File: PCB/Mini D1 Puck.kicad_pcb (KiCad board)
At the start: 2 copper layers, 32 x 36 mm, 14 parts, among them J1 PinHeader_1x03_P2.54mm_Vertic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, Q1 2N2222, Q2 2n2222, SW1 SW_Slide_SPDT_Angled_CK_OS102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, U1 D1_mini_board

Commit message: PCB fixes/reset button
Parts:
- added R6: 10K, Resistor_THT:R_Axial_DIN0204_L3.6mm_D1.6mm_P5.08mm_Horizontal, F.Cu at (171.5, 83.0)
- added SW2: SW_PUSH_1P1T_6x3.5mm_H4.3_APEM_MJTP1243, Button_Switch_THT:SW_PUSH_1P1T_6x3.5mm_H4.3_APEM_MJTP1243, F.Cu at (192.8, 83.0)
- moved C1 0.50 mm to (192.8, 76.0)
- moved R1 0.50 mm to (197.0, 70.5)
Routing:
- net (no net): track 277.9 -> 342.8 mm

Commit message: PCB Update. These gerber files were ordered May 1 2025
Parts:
- removed the B at (181.8, 59.5)
- added B: , Connector_JST:JST_EH_S3B-EH_1x03_P2.50mm_Horizontal, F.Cu at (182.0, 59.5)
- moved M 2.50 mm to (193.2, 59.5)
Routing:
- net (no net): track 342.8 -> 363.3 mm

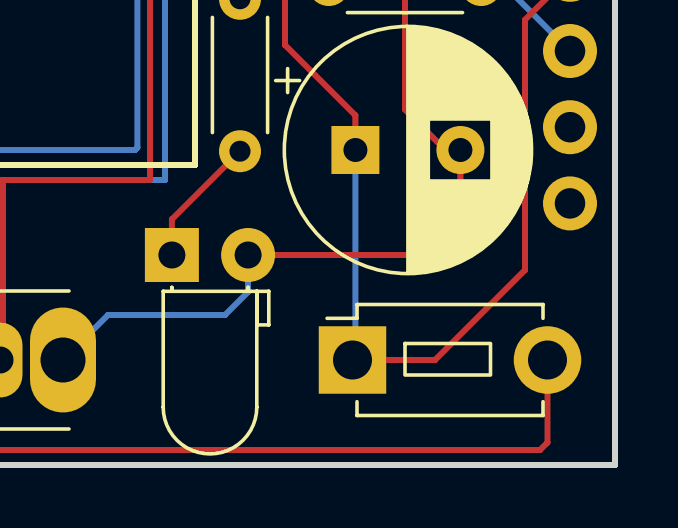
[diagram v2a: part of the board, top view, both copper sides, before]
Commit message: Case issues, silicone mold attempt, fix PCB reset button wiring
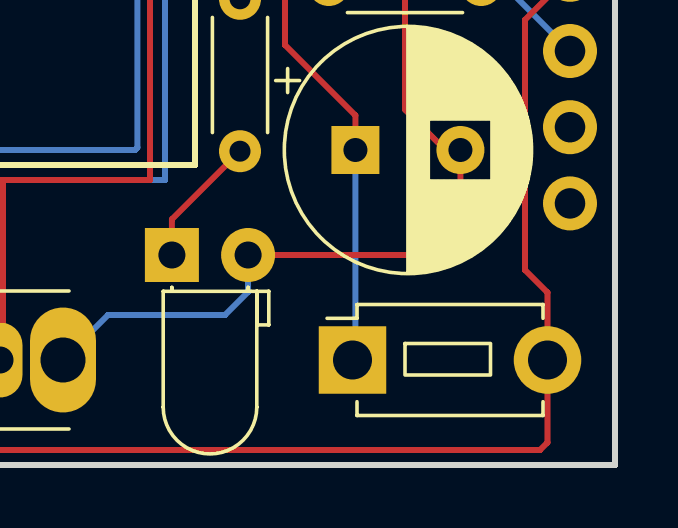
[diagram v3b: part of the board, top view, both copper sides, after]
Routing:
- net (no net): track 363.3 -> 359.6 mm
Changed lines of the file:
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@@
-	)
-	(segment
-		(start 192.75 83)
-		(end 195.5 83)
-		(width 0.2)
-		(layer "F.Cu")
-		(net 0)
 	)
 	(segment
@@
 		(start 171.5 59.42)
 		(end 171.5 58)
+		(width 0.2)
+		(layer "F.Cu")
+		(net 0)
+	)
+	(segment
+		(start 198.5 80)
+		(end 199.25 80.75)
 		(width 0.2)
 		(layer "F.Cu")
@@
 	)
 	(segment
-		(start 195.5 83)
-		(end 198.5 80)
+		(start 199.25 80.75)
+		(end 199.25 83)
 		(width 0.2)
 		(layer "F.Cu")

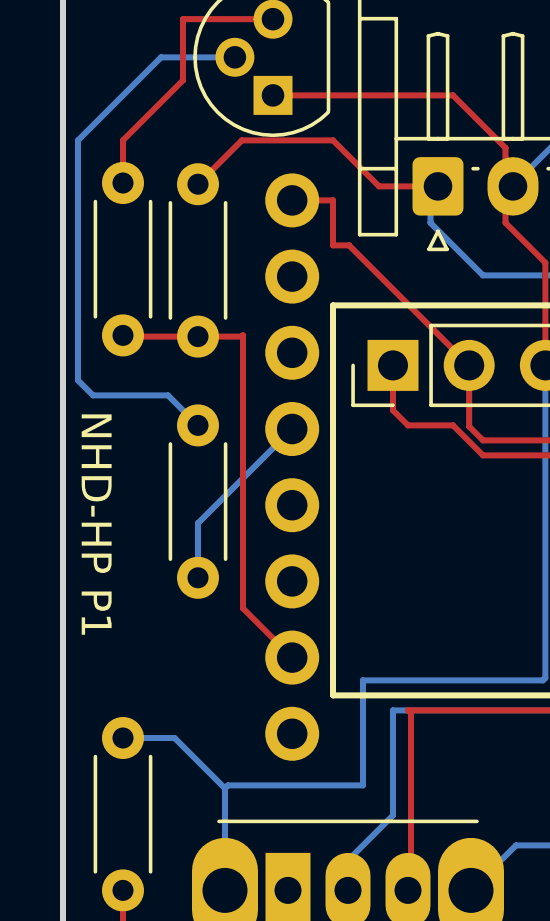
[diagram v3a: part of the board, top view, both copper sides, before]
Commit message: Fix battery monitor circuit, voltage divider not properly grounded
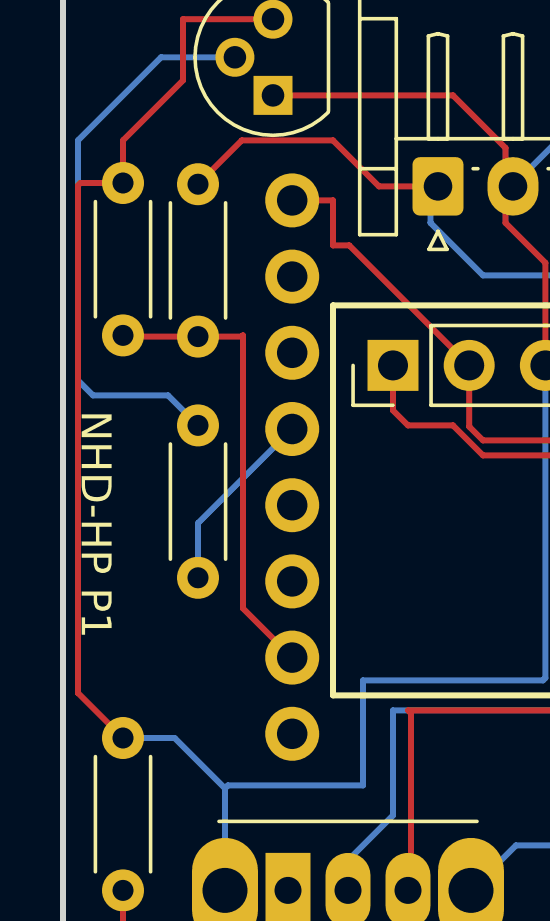
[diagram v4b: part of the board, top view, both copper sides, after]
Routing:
- net (no net): track 359.6 -> 380.2 mm
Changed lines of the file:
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@@
+	)
+	(segment
+		(start 170.08 59.42)
+		(end 170 59.5)
+		(width 0.2)
+		(layer "F.Cu")
+		(net 0)
 	)
 	(segment
@@
 	)
 	(segment
+		(start 171.5 59.42)
+		(end 170.08 59.42)
+		(width 0.2)
+		(layer "F.Cu")
+		(net 0)
+	)
+	(segment
 		(start 199.25 80.75)
 		(end 199.25 83)
@@
 	)
 	(segment
+		(start 170 76.42)
+		(end 171.5 77.92)
+		(width 0.2)
+		(layer "F.Cu")
+		(net 0)
+	)
+	(segment
 		(start 174 59.46)
 		(end 175.46 58)
@@
 		(width 0.2)
 		(layer "F.Cu")
+		(net 0)
+	)
+	(segment
+		(start 170 59.5)
+		(end 170 76.42)
+		(width 0.2)
+		(layer "F.Cu")

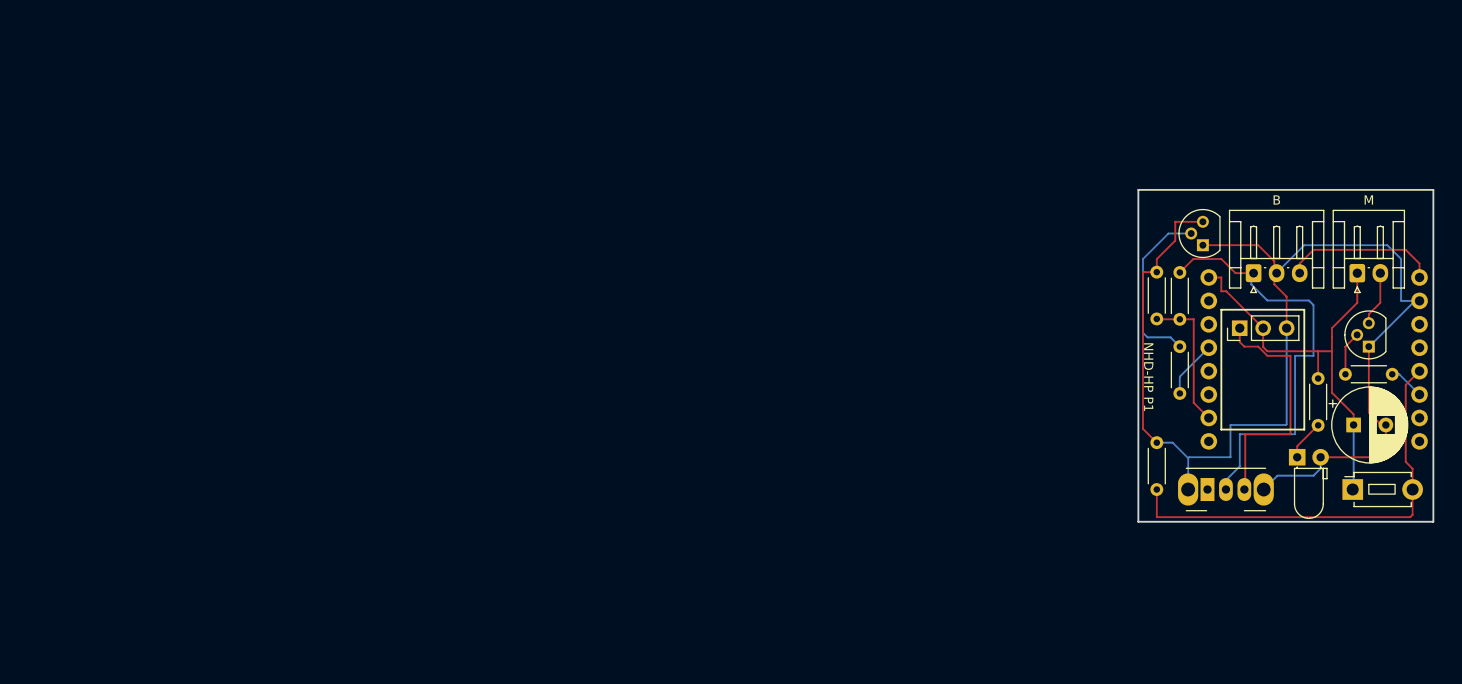
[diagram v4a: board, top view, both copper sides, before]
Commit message: Work on new schematic, up minimum voltage in firmware
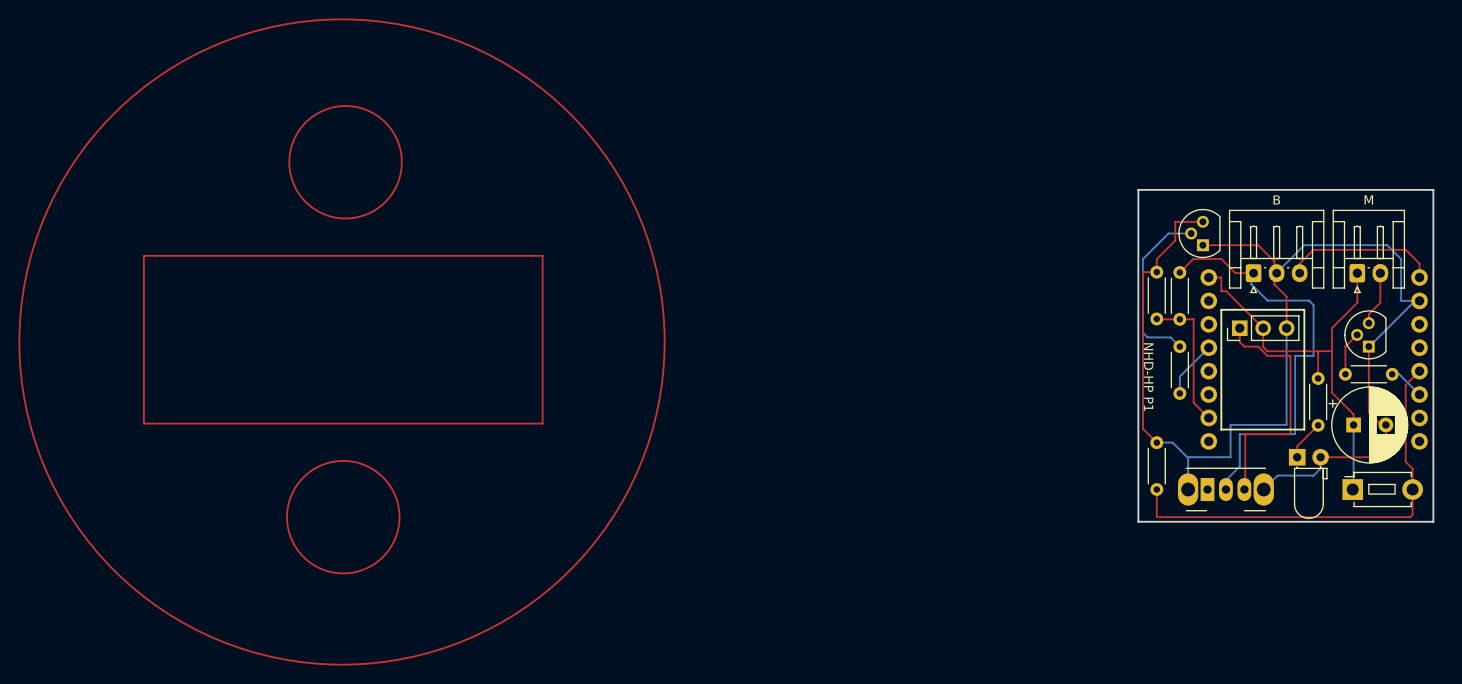
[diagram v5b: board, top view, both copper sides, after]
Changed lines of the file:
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@@
 		)
+	)
+	(gr_circle
+		(center 83.25 86)
+		(end 88.25 89.5)
+		(stroke
+			(width 0.2)
+			(type default)
+		)
+		(fill no)
+		(layer "F.Cu")
+	)
+	(gr_circle
+		(center 83.5 47.5)
+		(end 88.5 51)
+		(stroke
+			(width 0.2)
+			(type default)
+		)
+		(fill no)
+		(layer "F.Cu")
+	)
+	(gr_rect
+		(start 61.625 57.65)
+		(end 104.875 75.85)
+		(stroke
+			(width 0.2)
+			(type solid)
+		)
+		(fill no)
+		(layer "F.Cu")
+	)
+	(gr_circle
+		(center 83.11407 67)
+		(end 118.11407 67)
+		(stroke
+			(width 0.2)
+			(type solid)
+		)
+		(fill no)
+		(layer "F.Cu")
 	)
 	(gr_rect
